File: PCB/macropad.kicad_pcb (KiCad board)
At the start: 2 copper layers, 81.7 x 61.9 mm, 11 parts, among them SW10 SW_Push, SW11 SW_Push, SW12 SW_Push, SW2 RotaryEncoder_Switch, SW3 SW_Push, SW4 SW_Push, SW5 SW_Push, SW6 SW_Push, SW7 SW_Push, SW8 SW_Push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

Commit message: Redesign
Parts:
- added D1: 1N4148, Diode_THT:D_DO-35_SOD27_P7.62mm_Horizontal, F.Cu at (114.9, 50.3)
- added D10: 1N4148, Diode_THT:D_DO-35_SOD27_P7.62mm_Horizontal, F.Cu at (115.0, 107.5)
- added D11: 1N4148, Diode_THT:D_DO-35_SOD27_P7.62mm_Horizontal, F.Cu at (133.3, 107.4)
- added D12: 1N4148, Diode_THT:D_DO-35_SOD27_P7.62mm_Horizontal, F.Cu at (152.4, 107.5)
- added D2: 1N4148, Diode_THT:D_DO-35_SOD27_P7.62mm_Horizontal, F.Cu at (133.4, 50.3)
- added D3: 1N4148, Diode_THT:D_DO-35_SOD27_P7.62mm_Horizontal, F.Cu at (152.4, 50.3)
- added D4: 1N4148, Diode_THT:D_DO-35_SOD27_P7.62mm_Horizontal, F.Cu at (115.0, 69.3)
- added D5: 1N4148, Diode_THT:D_DO-35_SOD27_P7.62mm_Horizontal, F.Cu at (133.3, 69.3)
- added D6: 1N4148, Diode_THT:D_DO-35_SOD27_P7.62mm_Horizontal, F.Cu at (152.4, 69.3)
- added D7: 1N4148, Diode_THT:D_DO-35_SOD27_P7.62mm_Horizontal, F.Cu at (115.0, 88.4)
- added D8: 1N4148, Diode_THT:D_DO-35_SOD27_P7.62mm_Horizontal, F.Cu at (133.3, 88.4)
- added D9: 1N4148, Diode_THT:D_DO-35_SOD27_P7.62mm_Horizontal, F.Cu at (152.4, 88.4)
- added SW1: SW_Push, Button_Switch_Keyboard:SW_Cherry_MX_1.00u_PCB, F.Cu at (126.4, 40.2)
- added SW13: SW_Push, Button_Switch_Keyboard:SW_Cherry_MX_1.00u_PCB, F.Cu at (164.5, 97.3)
- added SW9: SW_Push, Button_Switch_Keyboard:SW_Cherry_MX_1.00u_PCB, F.Cu at (145.4, 97.3)
- moved SW5 38.5 mm to (145.4, 59.2)
- moved SW6 32.0 mm to (126.4, 78.3)
- moved SW8 23.9 mm to (126.4, 97.3)
- moved SW3 22.0 mm to (145.4, 40.2)
- moved SW10 17.3 mm to (164.5, 40.2)
- moved SW12 17.3 mm to (164.5, 78.3)
- moved SW4 17.3 mm to (126.4, 59.2)
- moved SW11 17.3 mm to (164.5, 59.2)
- moved U1 16.0 mm to (183.4, 45.1)
- moved SW7 5.32 mm to (145.4, 78.3)
- moved SW2 4.56 mm to (176.1, 99.9)
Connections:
- SW10 pad 1: GND -> COL3
- SW10 pad 2: Net-(U1-GPIO2/SCK) -> Net-(D3-A)
- SW11 pad 1: GND -> COL3
- SW11 pad 2: Net-(U1-GPIO4/MISO) -> Net-(D6-A)
- SW12 pad 1: GND -> COL3
- SW12 pad 2: Net-(U1-GPIO3/MOSI) -> Net-(D9-A)
- SW2 pad A: Net-(U1-GPIO1/RX) -> Net-(U1-GPIO2/SCK)
- SW2 pad B: Net-(U1-GPIO0/TX) -> Net-(U1-GPIO1/RX)
- SW2 pad S1: GND -> Net-(U1-GPIO4/MISO)
- SW2 pad S2: Net-(U1-GPIO7/SCL) -> GND
- SW3 pad 1: GND -> COL2
- SW3 pad 2: Net-(U1-GPIO26/ADC0/A0) -> Net-(D2-A)
- SW4 pad 1: GND -> COL1
- SW4 pad 2: Net-(U1-GPIO29/ADC3/A3) -> Net-(D4-A)
- SW5 pad 1: GND -> COL2
- SW5 pad 2: Net-(U1-GPIO27/ADC1/A1) -> Net-(D5-A)
- SW6 pad 1: GND -> COL1
- SW6 pad 2: Net-(U1-GPIO28/ADC2/A2) -> Net-(D7-A)
- SW7 pad 1: GND -> COL2
- SW7 pad 2: Net-(U1-GPIO6/SDA) -> Net-(D8-A)
- SW8 pad 1: GND -> COL1
- SW8 pad 2: Net-(U1-3V3) -> Net-(D10-A)
- U1 pad 1: Net-(U1-GPIO26/ADC0/A0) -> COL1
- U1 pad 11: Net-(U1-GPIO3/MOSI) -> unconnected-(U1-GPIO3/MOSI-Pad11)
- U1 pad 12: Net-(U1-3V3) -> unconnected-(U1-3V3-Pad12)
- U1 pad 2: Net-(U1-GPIO27/ADC1/A1) -> COL2
- U1 pad 3: Net-(U1-GPIO28/ADC2/A2) -> COL3
- U1 pad 4: Net-(U1-GPIO29/ADC3/A3) -> ROW1
- U1 pad 5: Net-(U1-GPIO6/SDA) -> ROW2
- U1 pad 6: Net-(U1-GPIO7/SCL) -> ROW3
- U1 pad 7: Net-(U1-GPIO0/TX) -> ROW4
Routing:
- net ROW4: track 0.00 -> 113.0 mm
- net COL1: track 0.00 -> 108.0 mm
- net ROW3: track 0.00 -> 98.5 mm
- net GND: track 223.6 -> 131.3 mm
- net COL2: track 0.00 -> 88.6 mm
- net Net-(U1-GPIO27/ADC1/A1): track 84.9 -> 0.00 mm
- net ROW2: track 0.00 -> 81.6 mm
- net Net-(U1-3V3): track 75.8 -> 0.00 mm
- net COL3: track 0.00 -> 69.4 mm
- net ROW1: track 0.00 -> 63.1 mm
- net Net-(U1-GPIO29/ADC3/A3): track 61.3 -> 0.00 mm
- net Net-(U1-GPIO26/ADC0/A0): track 57.4 -> 0.00 mm
- net Net-(U1-GPIO3/MOSI): track 56.3 -> 0.00 mm, vias 1 -> 0
- net Net-(U1-GPIO6/SDA): track 41.2 -> 0.00 mm
- net Net-(U1-GPIO7/SCL): track 40.3 -> 0.00 mm
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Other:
- board size 81.7 x 61.9 mm -> 81.9 x 78.7 mm
- board text added: "MATPAD V1.1"
- board text removed: "MatPad"

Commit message: update
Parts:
- added D13: 1N4148, Diode_THT:D_DO-35_SOD27_P7.62mm_Horizontal, F.Cu at (150.1, 47.9)
- added D14: 1N4148, Diode_THT:D_DO-35_SOD27_P7.62mm_Horizontal, F.Cu at (149.7, 67.0)
- added D15: 1N4148, Diode_THT:D_DO-35_SOD27_P7.62mm_Horizontal, F.Cu at (150.0, 86.0)
- added SW14: SW_Push, Button_Switch_Keyboard:SW_Cherry_MX_1.00u_PCB, F.Cu at (162.1, 37.8)
- added SW15: SW_Push, Button_Switch_Keyboard:SW_Cherry_MX_1.00u_PCB, F.Cu at (162.1, 56.8)
- added SW16: SW_Push, Button_Switch_Keyboard:SW_Cherry_MX_1.00u_PCB, F.Cu at (162.1, 75.9)
- moved SW2 23.9 mm to (152.3, 97.5)
- moved D1 21.6 mm to (93.5, 47.9)
- moved D10 21.6 mm to (93.6, 105.1)
- moved D11 21.6 mm to (111.9, 105.0)
- moved D12 21.6 mm to (131.0, 105.1)
- moved D2 21.6 mm to (112.0, 47.9)
- moved D3 21.6 mm to (131.0, 47.9)
- moved D4 21.6 mm to (93.6, 66.9)
- moved D5 21.6 mm to (111.9, 66.9)
- moved D6 21.6 mm to (131.0, 66.9)
- moved D7 21.6 mm to (93.6, 86.0)
- moved D8 21.6 mm to (111.9, 86.0)
- moved D9 21.6 mm to (131.0, 86.0)
- moved SW10 21.6 mm to (143.0, 37.8)
- moved SW11 21.6 mm to (143.0, 56.8)
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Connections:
- U1 pad 11: unconnected-(U1-GPIO3/MOSI-Pad11) -> COL4
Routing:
- net COL4: track 0.00 -> 63.2 mm
- net GND: track 131.3 -> 84.3 mm
- net Net-(U1-GPIO1/RX): track 58.4 -> 77.7 mm
- net ROW3: track 98.5 -> 116.0 mm
- net COL1: track 108.0 -> 125.2 mm
- net COL3: track 69.4 -> 86.5 mm
- net COL2: track 88.6 -> 105.2 mm
- net ROW2: track 81.6 -> 98.2 mm
- net ROW1: track 63.1 -> 79.5 mm
- net Net-(D14-A): track 0.00 -> 6.04 mm
- net ROW4: track 113.0 -> 119.0 mm
- net Net-(D15-A): track 0.00 -> 5.75 mm
- net Net-(D13-A): track 0.00 -> 5.64 mm
- net Net-(U1-GPIO2/SCK): track 59.5 -> 64.6 mm
- net Net-(U1-GPIO4/MISO): track 61.7 -> 66.1 mm
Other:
- board size 81.9 x 78.7 mm -> 97.8 x 80.9 mm

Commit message: Add files via upload
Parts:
- D1, D10, D11, D12, D13, D14, D15, D2, D3, D4, D5, D6, D7, D8, D9, U1: moved to B.Cu
- moved U1 18.4 mm to (159.6, 41.5), turned to 180 degrees
- moved D13 1.80 mm to (148.3, 47.9)
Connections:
- U1 pad 6: ROW3 -> ROW4
- U1 pad 7: ROW4 -> ROW3
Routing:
- net Net-(U1-GPIO1/RX): track 77.7 -> 56.3 mm
- net COL4: track 63.2 -> 50.2 mm
- net ROW3: track 116.0 -> 105.4 mm
- net GND: track 84.3 -> 93.2 mm
- net Net-(U1-GPIO2/SCK): track 64.6 -> 68.5 mm
- net COL3: track 86.5 -> 83.0 mm
- net COL2: track 105.2 -> 101.9 mm
- net COL1: track 125.2 -> 122.1 mm
- net ROW1: track 79.5 -> 76.4 mm
- net ROW4: track 119.0 -> 121.9 mm
- net ROW2: track 98.2 -> 95.3 mm
- net Net-(D13-A): track 5.64 -> 7.44 mm
- net Net-(U1-GPIO4/MISO): track 66.1 -> 64.6 mm
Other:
- board size 97.8 x 80.9 mm -> 81.1 x 81 mm
- board text removed: "MATPAD V1.1"

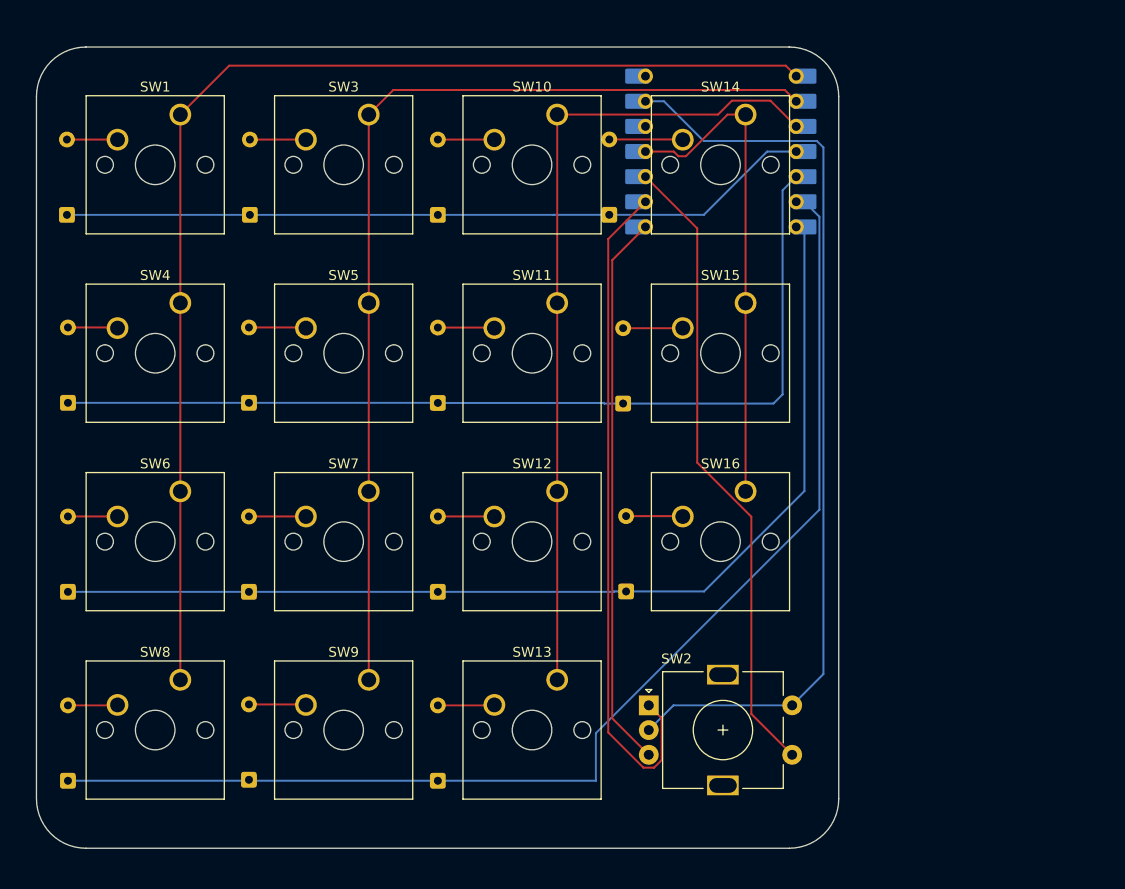
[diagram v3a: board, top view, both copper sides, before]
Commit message: Added vias for ground plane
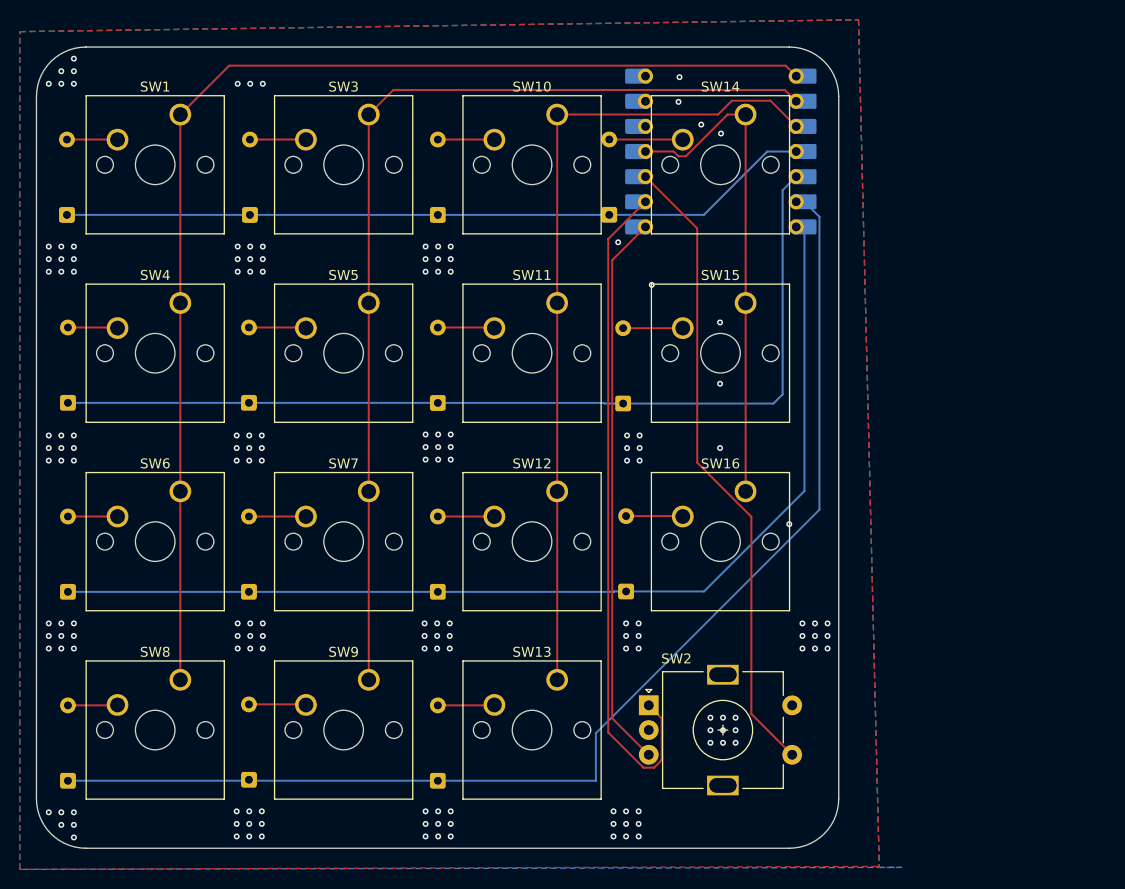
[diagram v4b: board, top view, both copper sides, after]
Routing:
- net GND: track 93.2 -> 0.00 mm, vias 0 -> 163
- added copper zone on B.Cu, net GND
- added copper zone on F.Cu, net GND
